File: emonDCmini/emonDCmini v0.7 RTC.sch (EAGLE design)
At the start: 25 parts

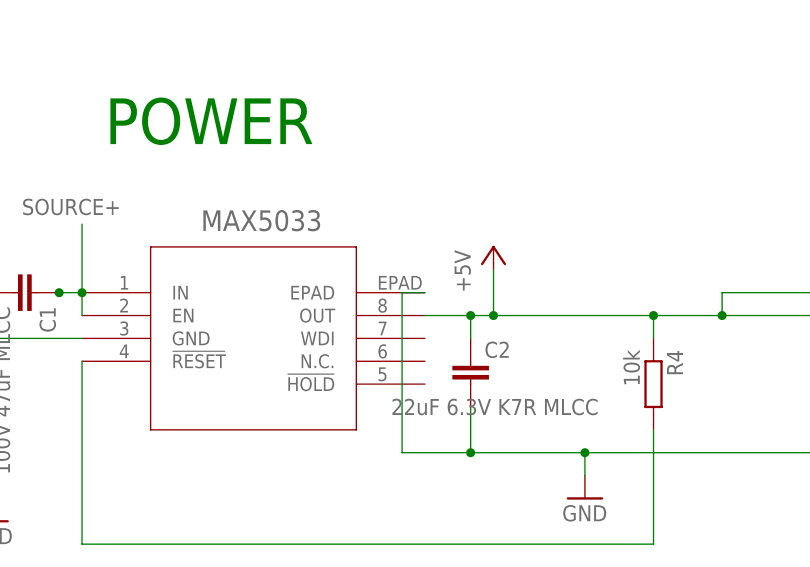
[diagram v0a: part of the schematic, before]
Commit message: new boards and library files
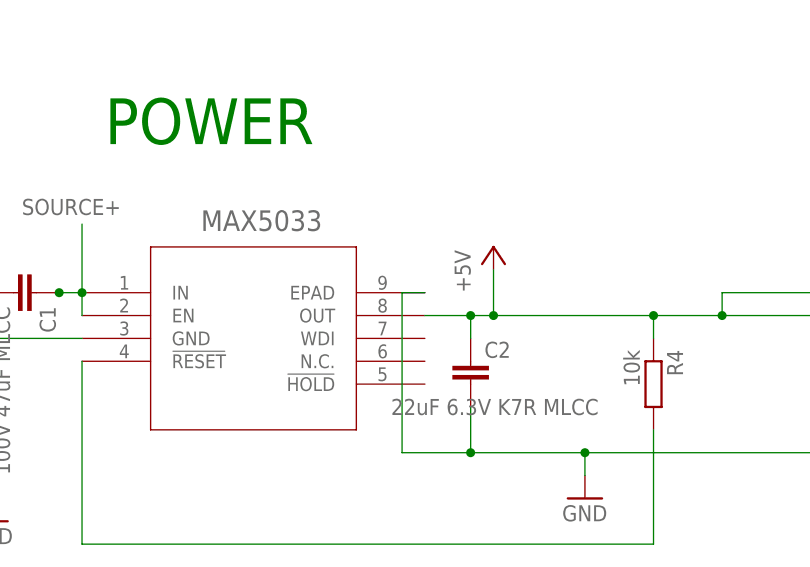
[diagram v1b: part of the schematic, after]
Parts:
- MAX5033: value MAX5023TASA-T21-0111D_SBE-14-L -> MAX5033BUSA+; device MAX5053:MAX5023TASA-T21-0111D_SBE-14-L -> MAX5033:MAX5033BUSA+; MANUFACTURER_PART_NUMBER max5033 -> (none)
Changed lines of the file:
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@@
 <?xml version="1.0" encoding="utf-8"?>
 <!DOCTYPE eagle SYSTEM "eagle.dtd">
-<eagle version="7.7.0">
+<eagle version="8.3.2">
 <drawing>
 <settings>
 <setting alwaysvectorfont="no"/>
+<setting keepoldvectorfont="yes"/>
 <setting verticaltext="up"/>
 </settings>
@@
 <part name="P+5" library="SparkFun" deviceset="3.3V" device=""/>
 <part name="R7" library="rcl" deviceset="R-EU_" device="R0603" value="10k"/>
-<part name="MAX5033" library="MAX5053" deviceset="MAX5023TASA-T" device="21-0111D_SBE-14-L" value="MAX5023TASA-T21-0111D_SBE-14-L">
-<attribute name="MANUFACTURER_PART_NUMBER" value="max5033"/>
-</part>
+<part name="MAX5033" library="MAX5033" deviceset="MAX5033BUSA+" device="" value="MAX5033BUSA+"/>
 <part name="GND1" library="supply1" deviceset="GND" device=""/>
 <part name="GND2" library="supply1" deviceset="GND" device=""/>
